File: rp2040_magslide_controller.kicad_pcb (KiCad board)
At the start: 4 copper layers, 36.1 x 66.8 mm, 49 parts, among them J1 USB_B_Mini, J2 50-00174, J3 Conn_02x05_Odd_Even, J4 Conn_02x20_Odd_Even, SW1 SW_SPST, SW2 SW_SPST, U1 W25Q64JV, U2 AMS1117-3.3, U3 RP2040, U4 CD74HC4067SM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

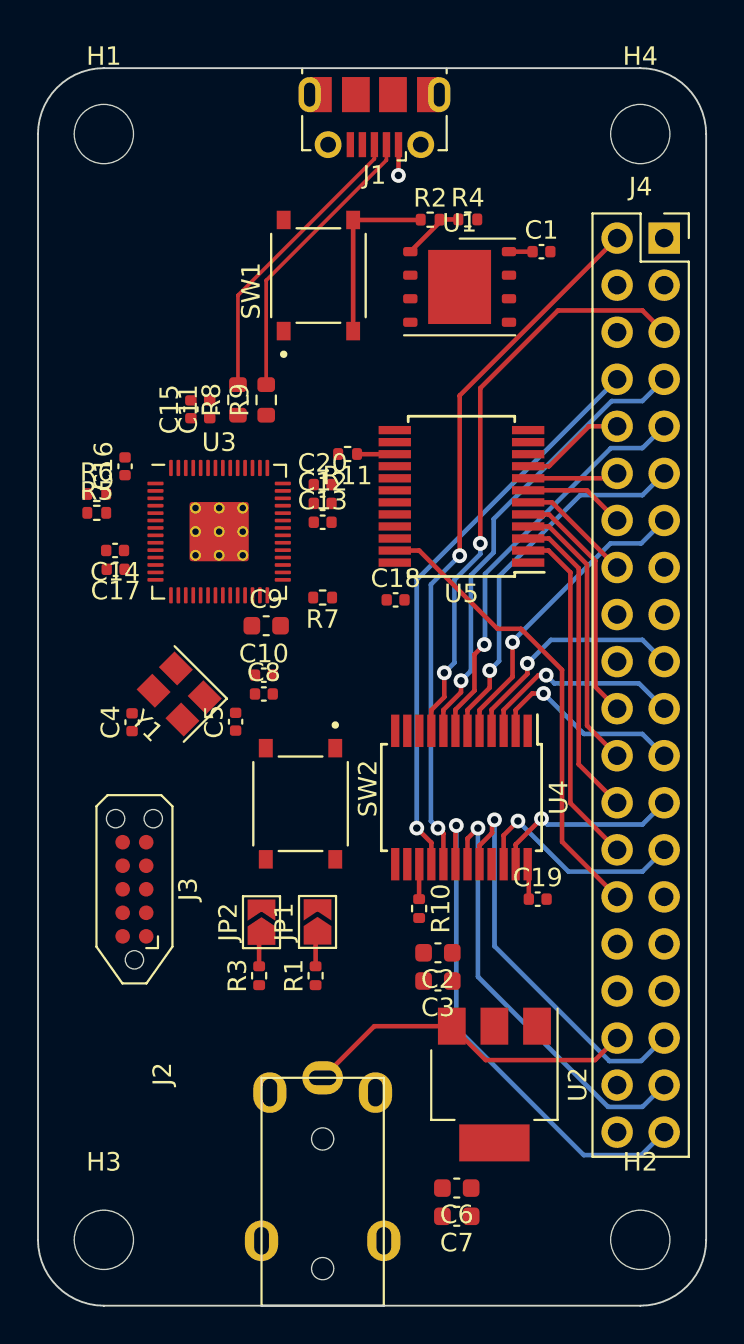
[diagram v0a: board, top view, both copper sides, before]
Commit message: Routing done, next up fix the JLCPCB-part numbers then order
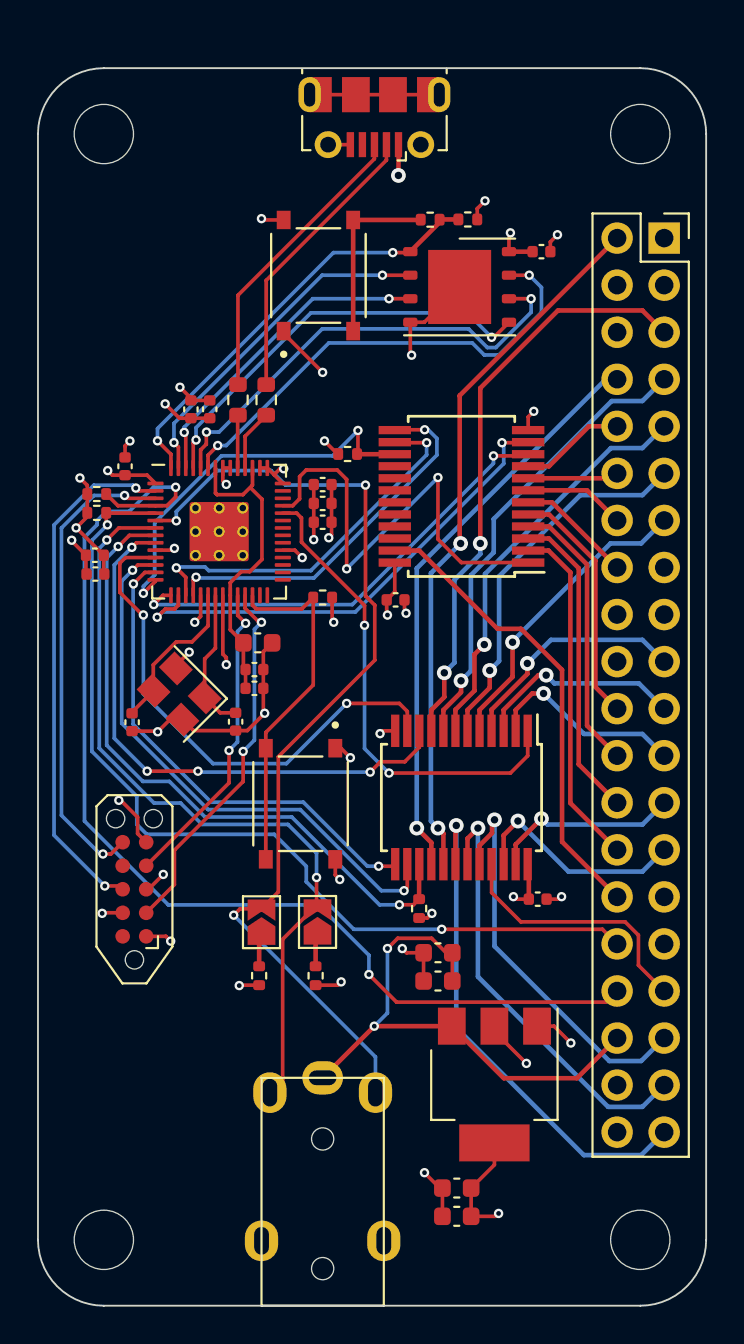
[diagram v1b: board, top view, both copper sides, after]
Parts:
- moved C14 1.12 mm to (164.1, 104.3)
- moved C17 1.12 mm to (164.1, 105.3)
- moved C9 1.03 mm to (172.9, 109.0)
- moved C10 0.59 mm to (172.7, 110.4)
- moved C8 0.59 mm to (172.7, 111.5)
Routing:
- net GND: track 0.00 -> 61.4 mm, vias 0 -> 26
- net extern_sda: track 0.00 -> 59.9 mm, vias 0 -> 2
- net board_sda: track 0.00 -> 53.1 mm, vias 0 -> 3
- net extern_scl: track 0.00 -> 50.0 mm, vias 0 -> 2
- net +3V3: track 3.19 -> 47.9 mm, vias 0 -> 20
- net board_scl: track 0.00 -> 42.5 mm, vias 0 -> 2
- net MUX0_EN: track 1.89 -> 35.7 mm, vias 0 -> 2
- net MUX_00: track 0.00 -> 30.7 mm, vias 0 -> 4
- net MUX_02: track 0.00 -> 30.3 mm, vias 0 -> 2
- net dbg_tx: track 0.00 -> 28.2 mm, vias 0 -> 2
- net MUX_01: track 0.00 -> 28.0 mm, vias 0 -> 2
- net MUX_11: track 0.00 -> 26.7 mm, vias 0 -> 2
- net MUX_03: track 0.00 -> 26.4 mm, vias 0 -> 2
- net ADC_0: track 0.00 -> 26.1 mm, vias 0 -> 2
- net dbg_rx: track 0.00 -> 25.8 mm, vias 0 -> 2
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- added copper zone on In1.Cu, net +3V3
- added copper zone on In2.Cu, net GND
